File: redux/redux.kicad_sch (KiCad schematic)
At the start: 249 parts, among them J14 Backplane, J3 Common, J4 Ext-2, J5 Ext-1, J6 Master, J7 Ext+1, J8 Ext+2, M1000 Bracket, Q1 MMBT3906, U1 MC100LVEL16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

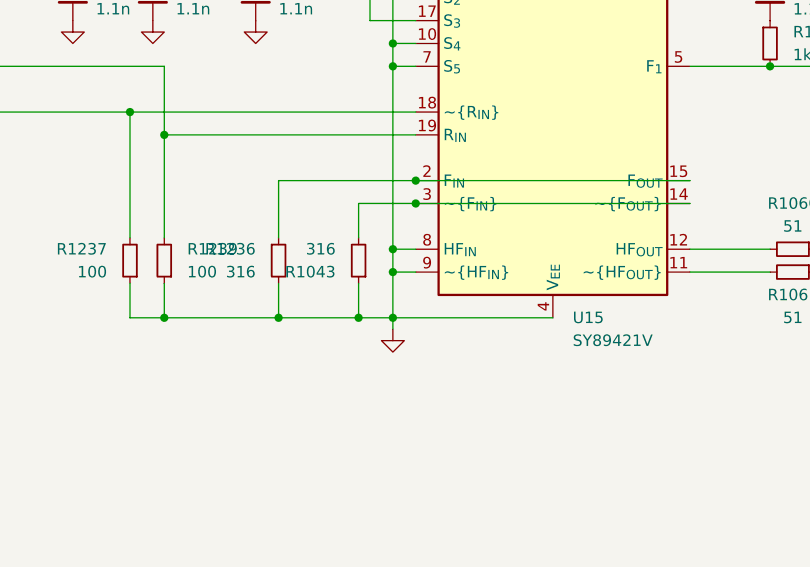
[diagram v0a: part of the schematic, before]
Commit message: Fix SY89421V pin 9 held low instead of floating
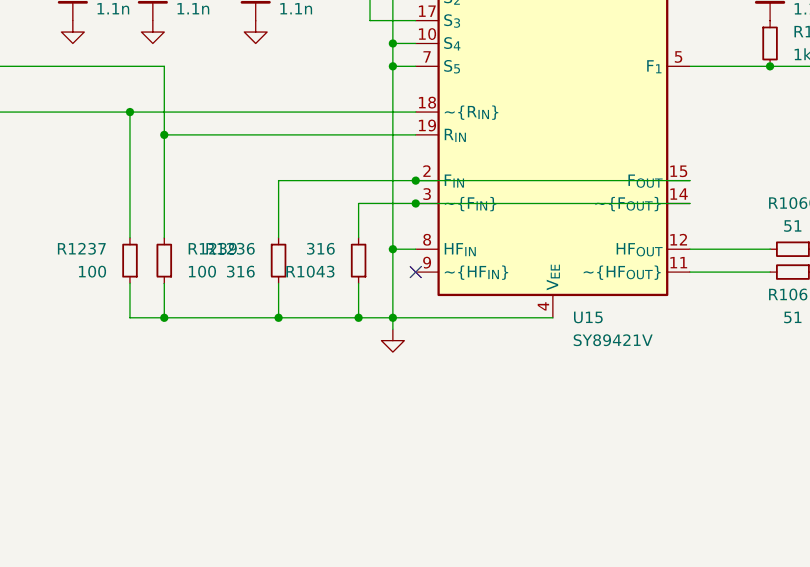
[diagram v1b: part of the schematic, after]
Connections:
- net GND: no longer U15.9 (~{HF_{IN}})
- no-connect marks 31 -> 32
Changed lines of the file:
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@@
 	)
 	(junction
-		(at 554.99 72.39)
-		(diameter 0)
-		(color 0 0 0 0)
-	)
-	(junction
 		(at 83.82 54.61)
 		(diameter 0)
@@
 	)
 	(no_connect
+		(at 557.53 72.39)
+	)
+	(no_connect
 		(at 532.13 316.23)
 	)
@@
 	(wire
 		(pts
-			(xy 554.99 72.39) (xy 554.99 77.47)
+			(xy 554.99 69.85) (xy 554.99 77.47)
 		)
 		(stroke
@@
 		)
 	)
-	(wire
-		(pts
-			(xy 557.53 72.39) (xy 554.99 72.39)
-		)
-		(stroke
-			(width 0)
-			(type default)
-		)
-	)
 	(bus
 		(pts
@@
 		)
 		(stroke
-			(width 0)
-			(type default)
-		)
-	)
-	(wire
-		(pts
-			(xy 554.99 69.85) (xy 554.99 72.39)
-		)
-		(stroke

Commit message: rev 0 (submitted to jlc)
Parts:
- C1098, C1230, C1242: value 51n -> 1u
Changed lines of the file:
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@@
 			)
 		)
-		(property "Value" "51n"
+		(property "Value" "1u"
 			(at 290.83 165.1062 0)
 			(effects
@@
 			)
 		)
-		(property "Value" "51n"
+		(property "Value" "1u"
 			(at 323.85 167.6462 0)
 			(effects
@@
 			)
 		)
-		(property "Value" "51n"
+		(property "Value" "1u"
 			(at 363.22 184.1562 0)
 			(effects
